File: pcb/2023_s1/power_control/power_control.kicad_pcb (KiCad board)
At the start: 2 copper layers, 26 parts, among them J1 Conn_01x05_Male, Q1 TIP122, Q2 TIP122, U1 40106, U2 4N25, U3 4N25

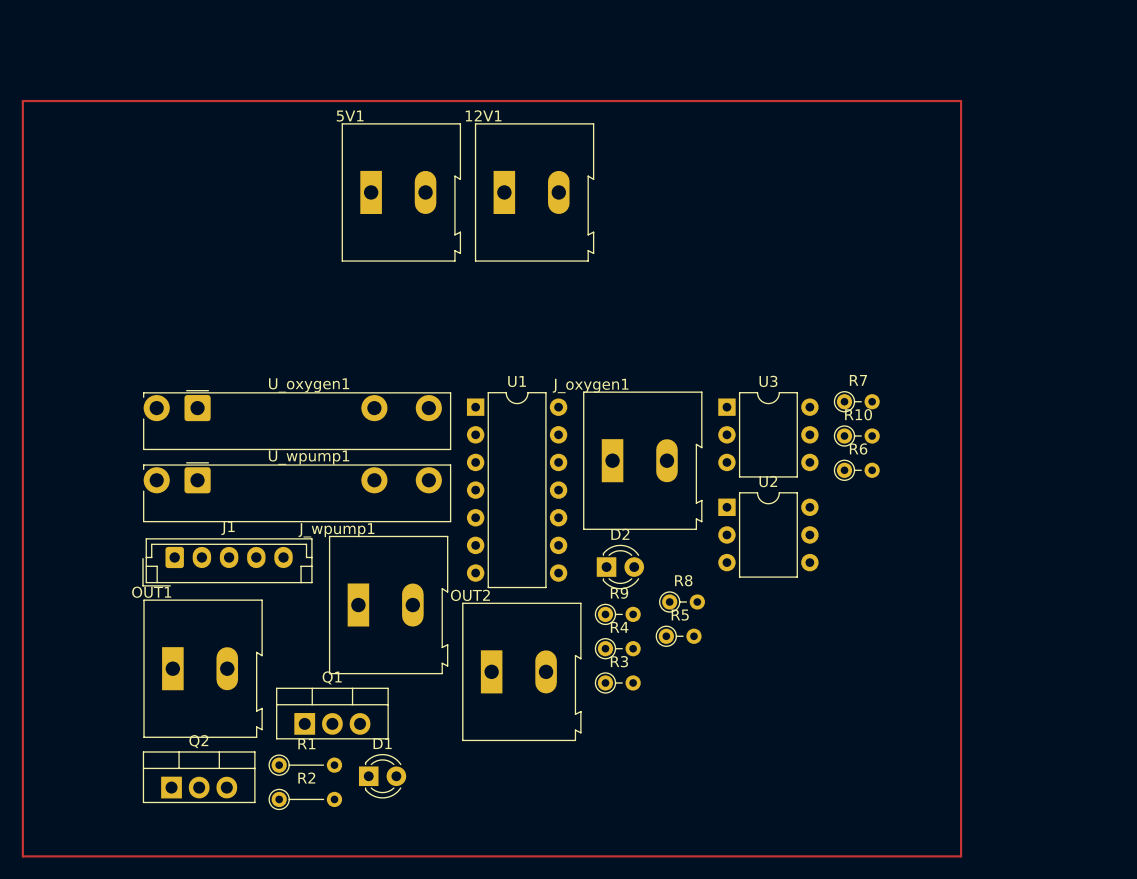
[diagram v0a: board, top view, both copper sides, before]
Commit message: corrected power control pcb, and repositioned most of the elements
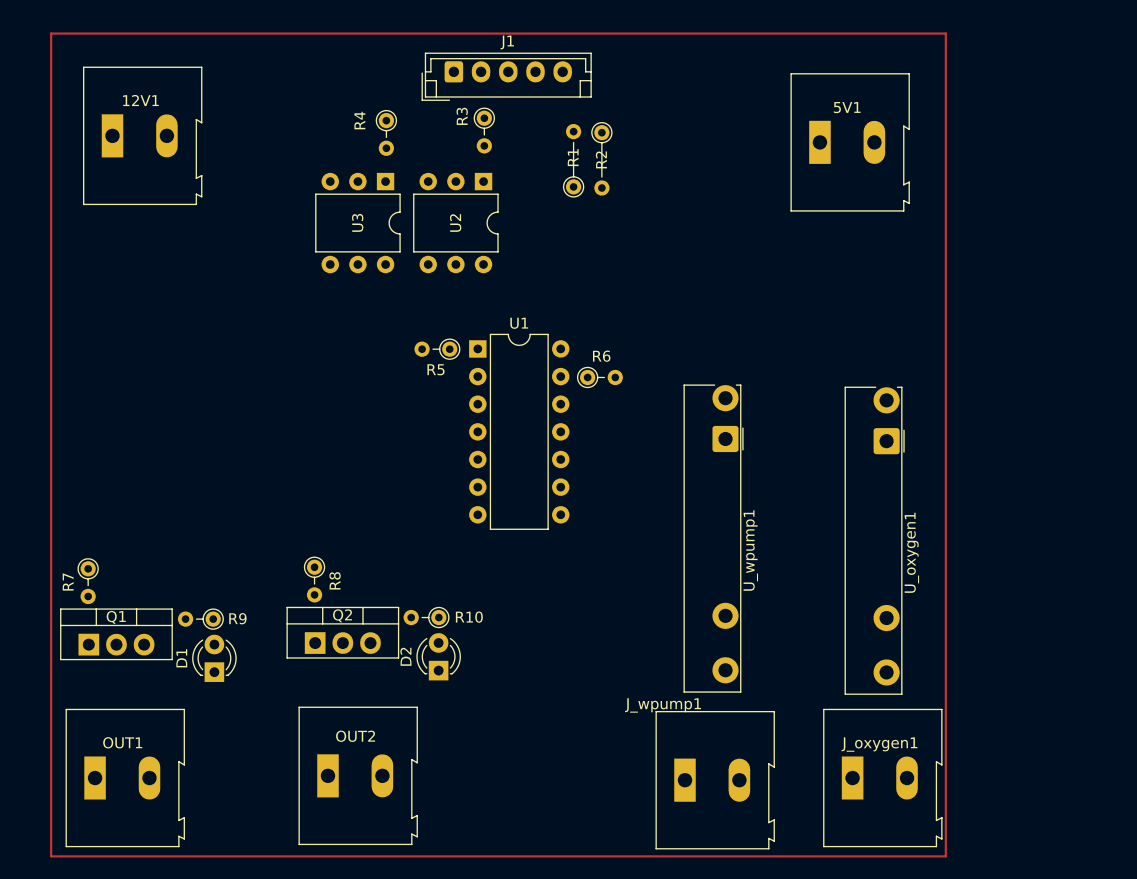
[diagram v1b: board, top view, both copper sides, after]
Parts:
- moved R7 71.2 mm to (109.6, 89.2), turned to -90 degrees
- moved R2 68.1 mm to (156.8, 49.1), turned to -90 degrees
- moved U_oxygen1 63.4 mm to (183.0, 77.5), turned to -90 degrees
- moved R1 59.6 mm to (154.2, 54.1), turned to 90 degrees
- moved R3 53.1 mm to (146.0, 47.8), turned to -90 degrees
- moved R4 52.5 mm to (137.0, 48.0), turned to -90 degrees
- moved J1 51.5 mm to (143.2, 43.5)
- moved U_wpump1 48.7 mm to (168.2, 77.2), turned to -90 degrees
- moved 5V1 41.5 mm to (176.8, 50.0)
- moved R10 40.8 mm to (141.8, 93.7), turned to 180 degrees
- moved U3 37.6 mm to (136.9, 53.6), turned to -90 degrees
- moved U2 37.4 mm to (145.9, 53.6), turned to -90 degrees
- moved J_oxygen1 36.6 mm to (179.8, 108.4)
- moved 12V1 36.4 mm to (111.8, 49.4)
- moved R9 36.0 mm to (121.1, 93.8), turned to 180 degrees
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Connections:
- R5 pad 2: 12v -> 5v
- U1 pad 7: GND -> GND5V
- U2 pad 4: GND12V -> GND5V

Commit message: update, finished connecting the power pcb module, and added the fan control to both pcbs
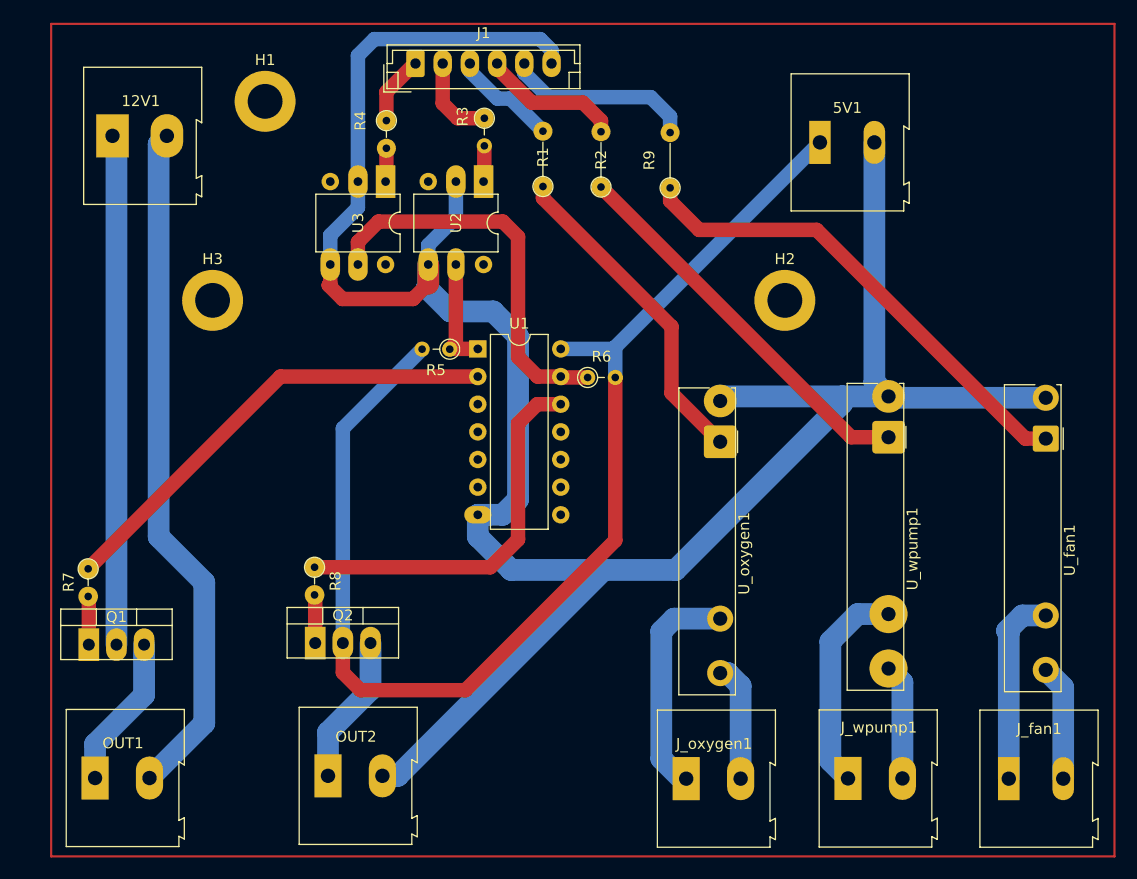
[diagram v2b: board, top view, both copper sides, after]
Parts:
- removed D1, D2: LED, LED_THT:LED_D3.0mm_Clear
- removed R10: 100, Resistor_THT:R_Axial_DIN0204_L3.6mm_D1.6mm_P2.54mm_Vertical
- added H1: MountingHole, MountingHole:MountingHole_3.2mm_M3_DIN965_Pad, F.Cu at (125.9, 46.2)
- added H2: MountingHole, MountingHole:MountingHole_3.2mm_M3_DIN965_Pad, F.Cu at (173.6, 64.5)
- added H3: MountingHole, MountingHole:MountingHole_3.2mm_M3_DIN965_Pad, F.Cu at (121.0, 64.5)
- added J_fan1: Screw_Terminal_01x02, TerminalBlock:TerminalBlock_Altech_AK300-2_P5.00mm, F.Cu at (194.2, 108.5)
- added U_fan1: 34.81-8240, OptoDevice:Finder_34.81, F.Cu at (197.6, 77.2)
- J1: value Conn_01x05_Male -> Conn_01x06_Male; footprint Connector_JST:JST_EH_B5B-EH-A_1x05_P2.50mm_Vertical -> Connector_JST:JST_EH_B6B-EH-A_1x06_P2.50mm_Vertical
- R9: value 100 -> R; footprint Resistor_THT:R_Axial_DIN0204_L3.6mm_D1.6mm_P2.54mm_Vertical -> Resistor_THT:R_Axial_DIN0204_L3.6mm_D1.6mm_P5.08mm_Vertical
- moved R9 57.7 mm to (163.1, 54.2), turned to 90 degrees
- moved J_oxygen1 15.3 mm to (164.5, 108.5)
- moved U_oxygen1 15.3 mm to (167.7, 77.5)
- moved J_wpump1 15.0 mm to (179.4, 108.4)
- moved U_wpump1 15.0 mm to (183.1, 77.1)
- moved R2 4.99 mm to (156.7, 54.1), turned to 90 degrees
- moved J1 3.61 mm to (139.7, 42.8)
- moved R1 2.82 mm to (151.4, 54.1)
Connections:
- J1 pad 5: GND5V -> D34
- R9 pad 2: Net-(OUT1-Pad1) -> D34
- U_oxygen1 pad A2: GND_SIG -> GND5V
- U_wpump1 pad A2: GND_SIG -> GND5V
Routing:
- net GND5V: track 0.00 -> 220.8 mm
- net 5v: track 0.00 -> 113.6 mm
- net GND12V: track 0.00 -> 63.1 mm
- net 12v: track 0.00 -> 46.9 mm
- net Net-(R9-Pad1): track 0.00 -> 44.8 mm
- net Net-(R7-Pad1): track 0.00 -> 43.1 mm
- net Net-(R6-Pad1): track 0.00 -> 36.3 mm
- net Net-(R2-Pad1): track 0.00 -> 35.9 mm
- net Net-(R8-Pad1): track 0.00 -> 35.1 mm
- net Net-(R1-Pad1): track 0.00 -> 30.2 mm
- net Net-(J_oxygen1-Pad1): track 0.00 -> 20.6 mm
- net Net-(J_wpump1-Pad1): track 0.00 -> 19.6 mm
- net Net-(J_fan1-Pad1): track 0.00 -> 17.8 mm
- net D34: track 0.00 -> 17.4 mm
- net Net-(OUT1-Pad1): track 0.00 -> 14.1 mm
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
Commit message: fix, separated the light control into another pcb, due to the different voltage it handles and confort for the use
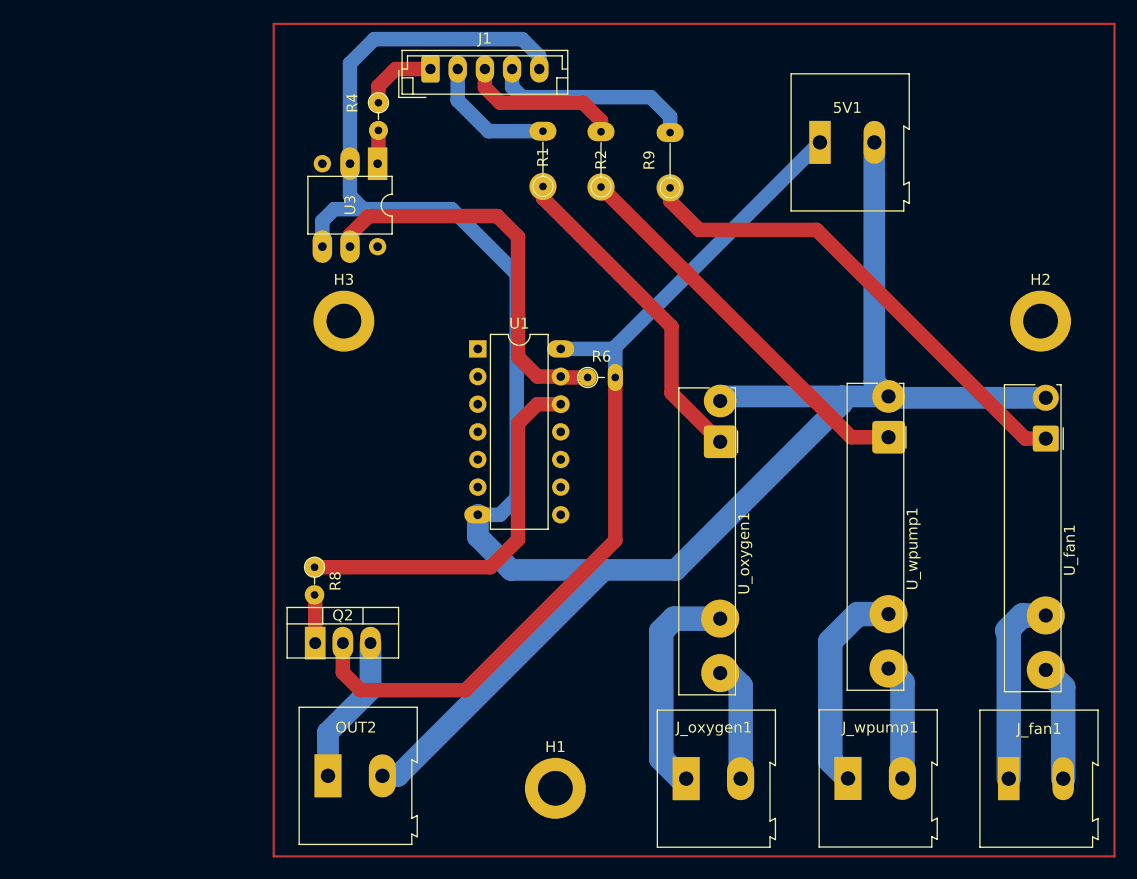
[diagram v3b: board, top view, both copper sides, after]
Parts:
- removed 12V1, OUT1: Screw_Terminal_01x02, TerminalBlock:TerminalBlock_Altech_AK300-2_P5.00mm
- removed Q1: TIP122, Package_TO_SOT_THT:TO-220-3_Vertical
- removed R3: 100, Resistor_THT:R_Axial_DIN0204_L3.6mm_D1.6mm_P2.54mm_Vertical
- removed R5: 10k, Resistor_THT:R_Axial_DIN0204_L3.6mm_D1.6mm_P2.54mm_Vertical
- removed R7: 10, Resistor_THT:R_Axial_DIN0204_L3.6mm_D1.6mm_P2.54mm_Vertical
- removed U2: 4N25, Package_DIP:DIP-6_W7.62mm
- J1: value Conn_01x06_Male -> Conn_01x05_Male; footprint Connector_JST:JST_EH_B6B-EH-A_1x06_P2.50mm_Vertical -> Connector_JST:JST_EH_B5B-EH-A_1x05_P2.50mm_Vertical
- moved H1 68.5 mm to (152.5, 109.3)
- moved H2 23.6 mm to (197.1, 66.4)
- moved H3 12.2 mm to (133.1, 66.4)
- moved R4 1.80 mm to (136.3, 46.4)
- moved U3 1.80 mm to (136.2, 52.0)
- moved J1 1.47 mm to (141.1, 43.3)
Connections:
- J1 pad 2: D26 -> D32
- J1 pad 3: D32 -> D33
- J1 pad 4: D33 -> D34
- J1 pad 5: D34 -> GND5V
- U1 pad 1: Net-(R5-Pad1) -> (no net)
- U1 pad 2: Net-(R7-Pad1) -> (no net)
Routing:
- net GND12V: track 63.1 -> 0.00 mm
- net 12v: track 46.9 -> 0.00 mm
- net Net-(R7-Pad1): track 43.1 -> 0.00 mm
- net 5v: track 113.6 -> 83.6 mm
- net Net-(OUT1-Pad1): track 14.1 -> 0.00 mm
- net GND5V: track 220.8 -> 208.2 mm
- net Net-(R5-Pad1): track 10.6 -> 0.00 mm
- net D26: track 8.05 -> 0.00 mm
- net Net-(Q1-Pad1): track 4.45 -> 0.00 mm
- net Net-(R3-Pad2): track 3.31 -> 0.00 mm
- net D32: track 9.70 -> 11.9 mm
- net D33: track 13.0 -> 14.6 mm
- net D34: track 17.4 -> 18.8 mm
- net D25: track 6.39 -> 6.96 mm
